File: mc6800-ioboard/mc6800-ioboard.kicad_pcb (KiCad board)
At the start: 2 copper layers, 26 parts, among them J1 Conn_01x02_Female, J2 Conn_01x39_Male, Q1 Q_NMOS_GSD, SW1 SW_Push, SW2 SW_Push, SW3 SW_Push, SW4 SW_Push, SW5 SW_Push, SW6 SW_Push, U1 74LS32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

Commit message: more routing
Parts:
- moved Q1 100.9 mm to (132.4, 142.4), turned to 180 degrees
- moved R2 100.2 mm to (135.6, 142.4), turned to 90 degrees
- moved J1 98.3 mm to (128.0, 141.1)
- moved RV1 73.9 mm to (130.2, 110.2)
- moved SW3 51.9 mm to (225.0, 108.0), turned to 90 degrees
- moved C3 43.3 mm to (150.6, 92.0), turned to 180 degrees
- moved SW2 40.7 mm to (131.0, 98.0), turned to 90 degrees
- moved DS1 35.5 mm to (148.1, 87.2)
- moved SW1 30.6 mm to (225.0, 88.0), turned to 90 degrees
- moved SW6 29.2 mm to (225.0, 118.0), turned to 90 degrees
- moved SW5 28.3 mm to (225.0, 98.0), turned to 90 degrees
- moved SW4 27.8 mm to (131.0, 88.0), turned to 90 degrees
- moved R3 4.56 mm to (134.1, 134.2)
- moved R4 4.56 mm to (134.1, 126.3)
- moved R1 4.56 mm to (133.9, 117.4)
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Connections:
- DS1 pad 13: (no net) -> Net-(DS1-Pad13)
- DS1 pad 14: (no net) -> Net-(DS1-Pad14)
- DS1 pad 15: (no net) -> Net-(DS1-Pad15)
- DS1 pad 16: (no net) -> Net-(DS1-Pad16)
- J2 pad 13: (no net) -> /A12
- J2 pad 14: (no net) -> /A13
- J2 pad 15: (no net) -> /A14
- J2 pad 16: (no net) -> /A15
- J2 pad 19: (no net) -> /M1
- J2 pad 22: (no net) -> /INT1
- J2 pad 23: (no net) -> /MEM_RQ
- J2 pad 25: (no net) -> /RO
- J2 pad 35: (no net) -> /RX
- J2 pad 36: (no net) -> /TX
- J2 pad 37: (no net) -> /USR1
- J2 pad 39: (no net) -> /USR3
- SW3 pad 1: /PB.5 -> /PB.4
- SW4 pad 1: /PB.5 -> /PB.4
- U3 pad 14: (no net) -> /PB.4
- U3 pad 40: (no net) -> /INTA
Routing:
- net /PB.6: track 0.00 -> 138.6 mm, vias 0 -> 3
- net /PB.2: track 0.00 -> 101.2 mm, vias 0 -> 2
- net /PB.7: track 0.00 -> 100.1 mm, vias 0 -> 3
- net /A3: track 0.00 -> 98.5 mm, vias 0 -> 1
- net /PB.1: track 0.00 -> 88.1 mm, vias 0 -> 2
- net /ADD_SEL: track 0.00 -> 86.8 mm, vias 0 -> 1
- net Net-(JP1-Pad2): track 0.00 -> 79.3 mm, vias 0 -> 2
- net /PB.0: track 0.00 -> 79.0 mm, vias 0 -> 2
- net /A1: track 0.00 -> 74.4 mm, vias 0 -> 1
- net /A0: track 0.00 -> 73.0 mm, vias 0 -> 1
- net /PB.5: track 0.00 -> 72.7 mm, vias 0 -> 4
- net /PB.3: track 0.00 -> 72.6 mm, vias 0 -> 2
- net /R_W: track 0.00 -> 64.4 mm, vias 0 -> 2
- net /A2: track 0.00 -> 60.5 mm, vias 0 -> 1
- net /E: track 0.00 -> 57.8 mm, vias 0 -> 2
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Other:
- board outline added: 102.5 x 70.5 mm

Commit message: routing mostly dome some tidying needeed
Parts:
- moved SW1 1.00 mm to (224.0, 88.0)
- moved SW3 1.00 mm to (224.0, 108.0)
- moved SW5 1.00 mm to (224.0, 98.0)
- moved SW6 1.00 mm to (224.0, 118.0)
- moved D1 0.50 mm to (127.9, 134.1)
- moved D2 0.50 mm to (127.8, 126.1)
- moved D3 0.50 mm to (127.8, 117.5)
- moved C1 0.50 mm to (161.5, 139.4)
- moved C2 0.50 mm to (223.4, 146.8)
- moved C3 0.50 mm to (150.1, 92.0)
- moved C4 0.50 mm to (161.5, 128.0)
- moved DS1 0.50 mm to (147.6, 87.2)
- moved J1 0.50 mm to (127.5, 141.1)
- moved J2 0.50 mm to (127.3, 150.7)
- moved JP1 0.50 mm to (218.6, 140.2)
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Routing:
- net +5V: track 79.8 -> 238.4 mm, vias 0 -> 2
- net /PB.7: track 100.1 -> 210.8 mm, vias 3 -> 4
- net /PB.4: track 49.3 -> 137.5 mm, vias 2 -> 3
- net /PB.3: track 72.6 -> 153.1 mm, vias 2 -> 4
- net Net-(DS1-Pad5): track 0.00 -> 45.3 mm, vias 0 -> 1
- net /PA.6: track 47.7 -> 84.3 mm, vias 0 -> 2
- net /PA.5: track 45.8 -> 79.7 mm, vias 0 -> 2
- net /PA.3: track 42.4 -> 74.6 mm, vias 0 -> 2
- net /PA.2: track 40.6 -> 72.7 mm, vias 0 -> 2
- net /PA.4: track 44.2 -> 75.7 mm, vias 0 -> 2
- net /PA.1: track 39.3 -> 70.5 mm, vias 0 -> 2
- net /PA.0: track 37.1 -> 68.2 mm, vias 0 -> 2
- net /A0: track 73.0 -> 74.1 mm
- net /PB.6: track 138.6 -> 137.6 mm
- net /R_W: track 64.4 -> 63.7 mm
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- added copper zone on B.Cu, net GND
- added copper zone on F.Cu, net GND
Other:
- board size 102.5 x 70.5 mm -> 102 x 70 mm

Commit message: sync checkpoint
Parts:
- Input interupt: renamed from JP1
- RV1: value R_POT -> Contrast
- SW1: value SW_Push -> C
- SW2: value SW_Push -> B
- SW3: value SW_Push -> E
- SW4: value SW_Push -> A
- SW5: value SW_Push -> D
- SW6: value SW_Push -> F
- U3: value 6822 -> MC6822
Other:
- outline, holes or cut-outs redrawn

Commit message: checkpoint sync
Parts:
- removed Input interupt: Jumper_NC_Small, Jumper:SolderJumper-2_P1.3mm_Bridged_RoundedPad1.0x1.5mm
- added J3: 10118193-0001LF, digikey-footprints:USB_Micro_B_Female_10118193-0001LF, F.Cu at (194.0, 85.8)
- added JP1: Jumper_NC_Small, Jumper:SolderJumper-2_P1.3mm_Bridged_RoundedPad1.0x1.5mm, B.Cu at (218.6, 140.3)
- DS1: value HY1602E -> WC1602A
- RV1: value Contrast -> R_POT
- SW1: value C -> SW_Push
- SW2: value B -> SW_Push
- SW3: value E -> SW_Push
- SW4: value A -> SW_Push
- SW5: value D -> SW_Push
- SW6: value F -> SW_Push
- U3: value MC6822 -> 6822
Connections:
- DS1 pad 10: /PA.1 -> /PA.3
- DS1 pad 11: /PA.2 -> Net-(DS1-Pad11)
- DS1 pad 12: /PA.3 -> Net-(DS1-Pad12)
- DS1 pad 15: Net-(DS1-Pad15) -> +5V
- DS1 pad 16: Net-(DS1-Pad16) -> GND
- DS1 pad 3: GND -> Net-(DS1-Pad3)
- DS1 pad 4: +5V -> /PA.6
- DS1 pad 5: Net-(DS1-Pad5) -> /PA.5
- DS1 pad 6: /PA.6 -> /PA.4
- DS1 pad 7: /PA.5 -> /PA.0
- DS1 pad 8: /PA.4 -> /PA.1
- DS1 pad 9: /PA.0 -> /PA.2
- RV1 pad 2: Net-(DS1-Pad5) -> Net-(DS1-Pad3)
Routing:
- net +5V: track 238.4 -> 288.7 mm
- net Net-(DS1-Pad3): track 0.00 -> 47.4 mm, vias 0 -> 1
- net Net-(DS1-Pad5): track 45.3 -> 0.00 mm, vias 1 -> 0
- net /PA.0: track 68.2 -> 53.5 mm
- net /PA.3: track 74.6 -> 64.8 mm
- net /PA.2: track 72.7 -> 66.2 mm
- net /PA.1: track 70.5 -> 64.1 mm
- net /PA.5: track 79.7 -> 82.3 mm
- net /PA.4: track 75.7 -> 77.8 mm
- net /PA.6: track 84.3 -> 86.4 mm

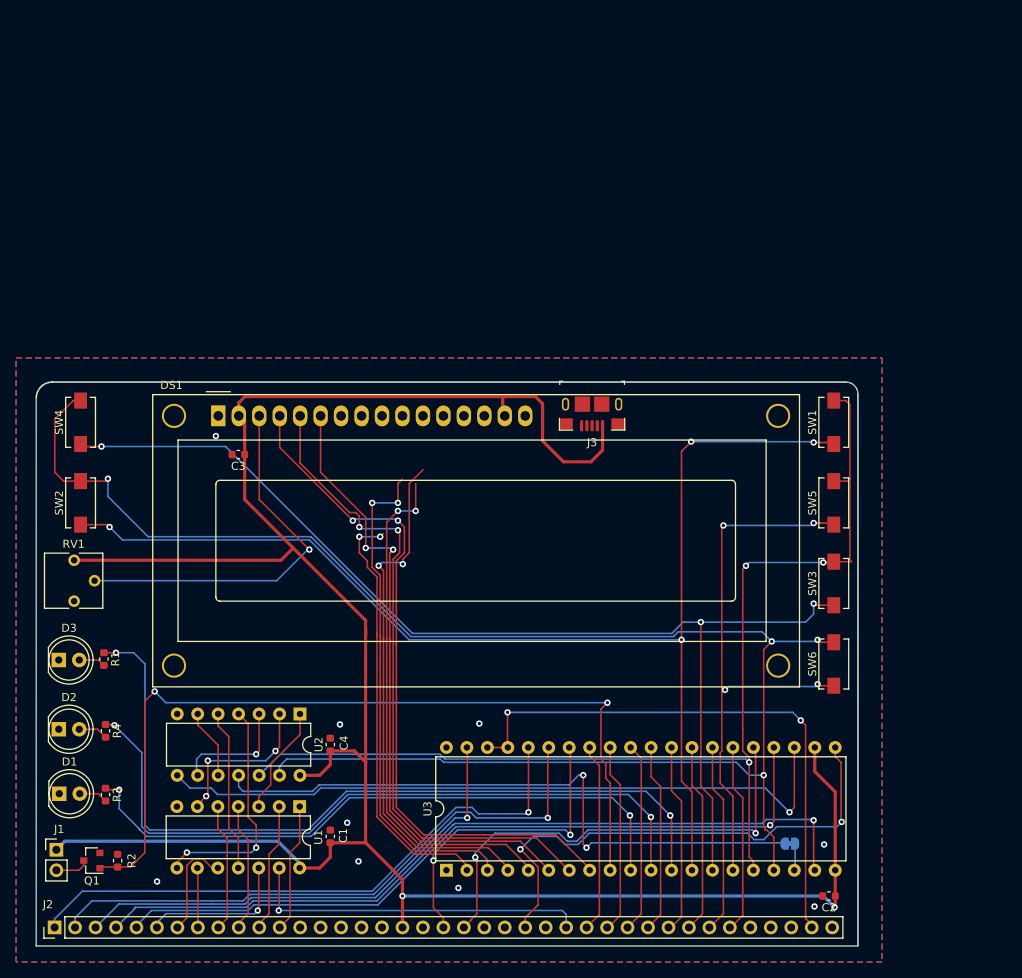
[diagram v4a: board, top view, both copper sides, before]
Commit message: reducing board size
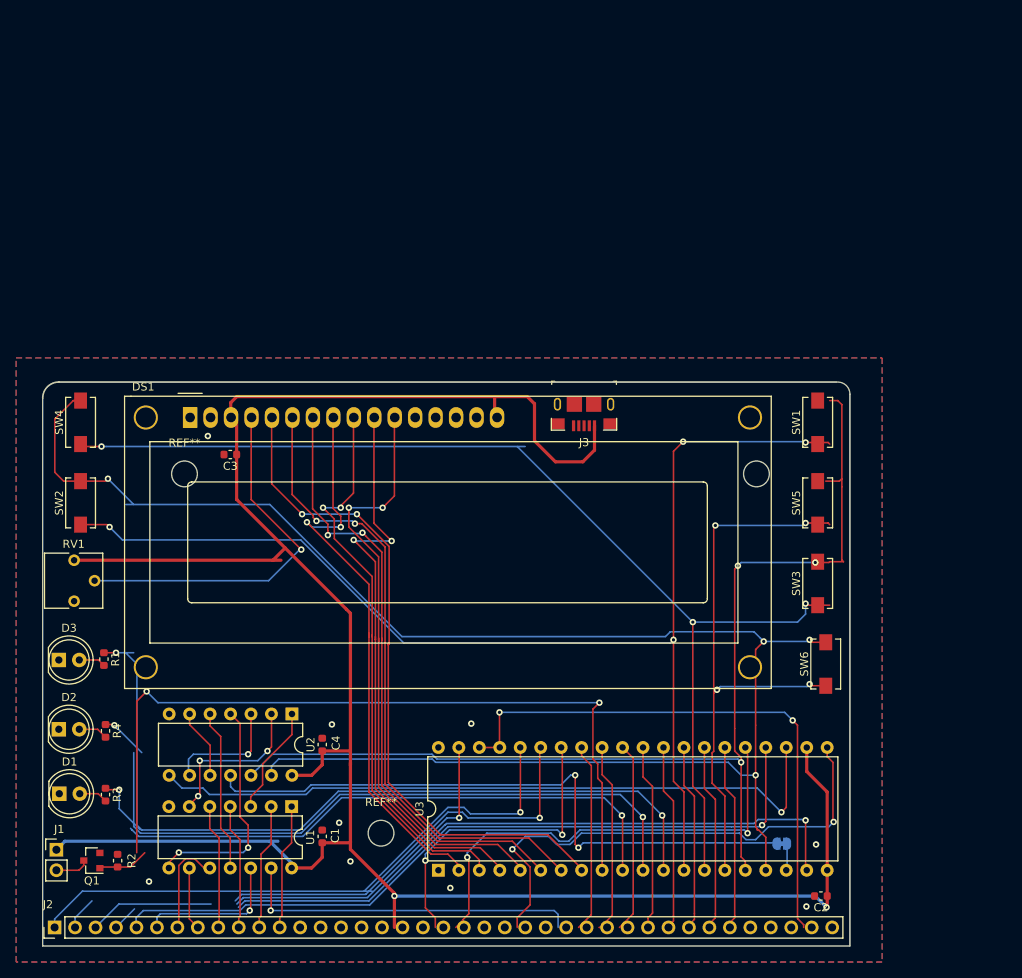
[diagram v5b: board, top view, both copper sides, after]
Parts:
- added REF**: MountingHole_3.2mm_M3_ISO7380, MountingHole:MountingHole_3.2mm_M3_ISO7380, F.Cu at (167.8, 139.0)
- added REF**: MountingHole_3.2mm_M3_ISO7380, MountingHole:MountingHole_3.2mm_M3_ISO7380, F.Cu at (214.4, 94.4)
- added REF**: MountingHole_3.2mm_M3_ISO7380, MountingHole:MountingHole_3.2mm_M3_ISO7380, F.Cu at (143.4, 94.4)
- moved DS1 3.51 mm to (144.1, 87.4)
- moved SW1 2.00 mm to (222.0, 88.0)
- moved SW3 2.00 mm to (222.0, 108.0)
- moved SW5 2.00 mm to (222.0, 98.0)
- moved C1 1.00 mm to (160.5, 139.4)
- moved C2 1.00 mm to (222.4, 146.8)
- moved C3 1.00 mm to (149.1, 92.0)
- moved C4 1.00 mm to (160.5, 128.0)
- moved J3 1.00 mm to (193.0, 85.8)
- moved JP1 1.00 mm to (217.6, 140.3)
- moved SW6 1.00 mm to (223.0, 118.0)
- moved U1 1.00 mm to (156.7, 135.7)
- moved U2 1.00 mm to (156.7, 124.2)
- moved U3 1.00 mm to (174.9, 143.6)
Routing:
- net /A1: track 74.4 -> 55.6 mm
- net /PA.0: track 53.5 -> 71.3 mm
- net /A3: track 98.5 -> 84.5 mm
- net /PA.3: track 64.8 -> 74.9 mm
- net /PA.1: track 64.1 -> 71.7 mm
- net /PA.2: track 66.2 -> 73.7 mm
- net /A2: track 60.5 -> 56.3 mm
- net /PA.5: track 82.3 -> 79.9 mm
- net +5V: track 288.7 -> 286.3 mm
- net /PA.6: track 86.4 -> 84.4 mm
- net /PB.7: track 210.8 -> 209.5 mm
- net /PB.4: track 137.5 -> 136.3 mm
- net /PA.4: track 77.8 -> 76.7 mm
- net Net-(DS1-Pad3): track 47.4 -> 46.4 mm
- net /PB.3: track 153.1 -> 152.4 mm
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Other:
- board size 102 x 70 mm -> 100.2 x 70 mm

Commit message: drc complete on io board and started logic for device select
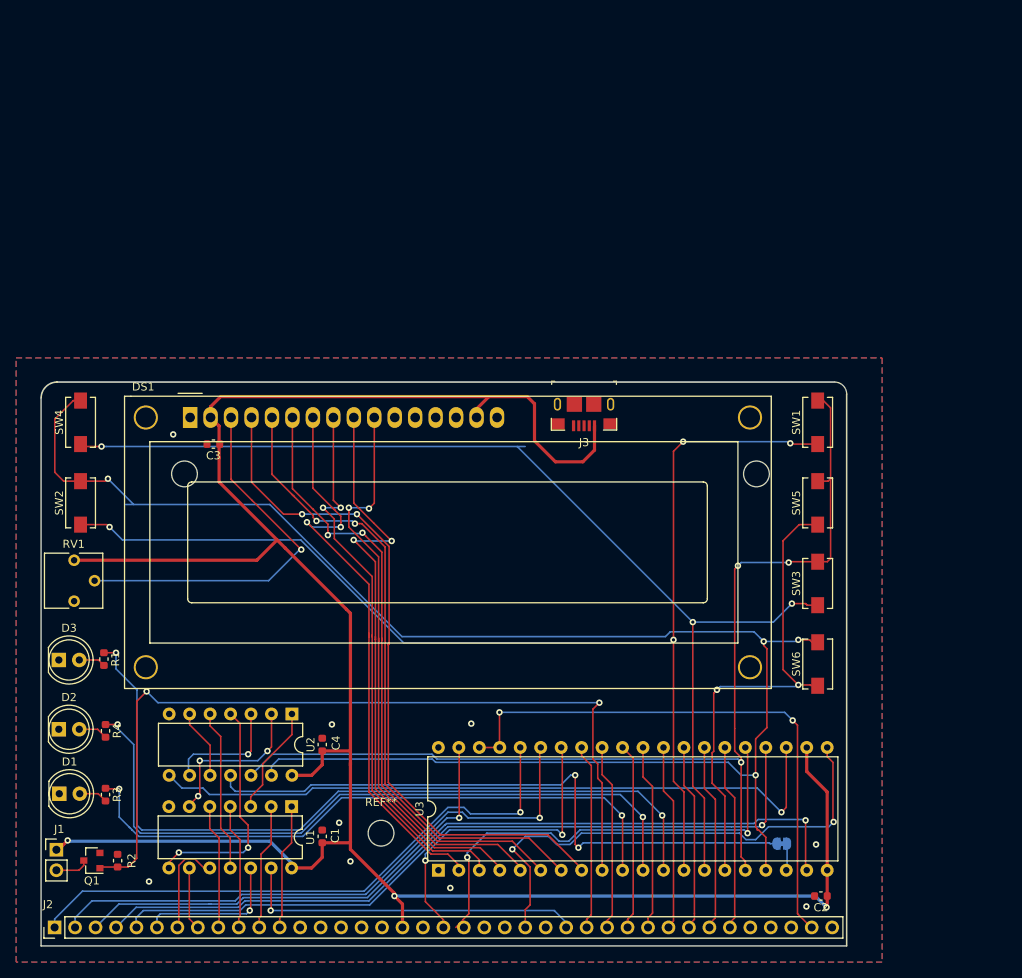
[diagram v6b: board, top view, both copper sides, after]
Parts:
- moved C3 2.47 mm to (147.0, 90.7)
- moved SW6 1.00 mm to (222.0, 118.0)
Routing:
- net /A1: track 55.6 -> 73.4 mm
- net /PB.5: track 73.0 -> 59.1 mm, vias 4 -> 2
- net /A3: track 84.5 -> 97.4 mm
- net /A2: track 56.3 -> 59.8 mm
- net /PB.6: track 137.6 -> 135.1 mm
- net /PB.4: track 136.3 -> 134.1 mm
- net /PA.6: track 84.4 -> 86.6 mm
- net /PA.2: track 73.7 -> 75.7 mm
- net +5V: track 286.3 -> 288.2 mm, vias 2 -> 3
- net Net-(DS1-Pad3): track 46.4 -> 48.3 mm
- net /PB.7: track 209.5 -> 207.6 mm
- net /PA.3: track 74.9 -> 73.1 mm
- net /PB.2: track 101.2 -> 99.5 mm
- net /PA.1: track 71.7 -> 70.0 mm
- net /PB.3: track 152.4 -> 150.9 mm
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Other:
- board size 100.2 x 70 mm -> 100 x 70 mm
